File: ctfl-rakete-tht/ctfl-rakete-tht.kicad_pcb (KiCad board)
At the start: 2 copper layers, 99.6 x 99.2 mm, 30 parts, among them J1 Conn_02x03_Odd_Even, SW1 SW_SPDT, U1 ATtiny212-SS

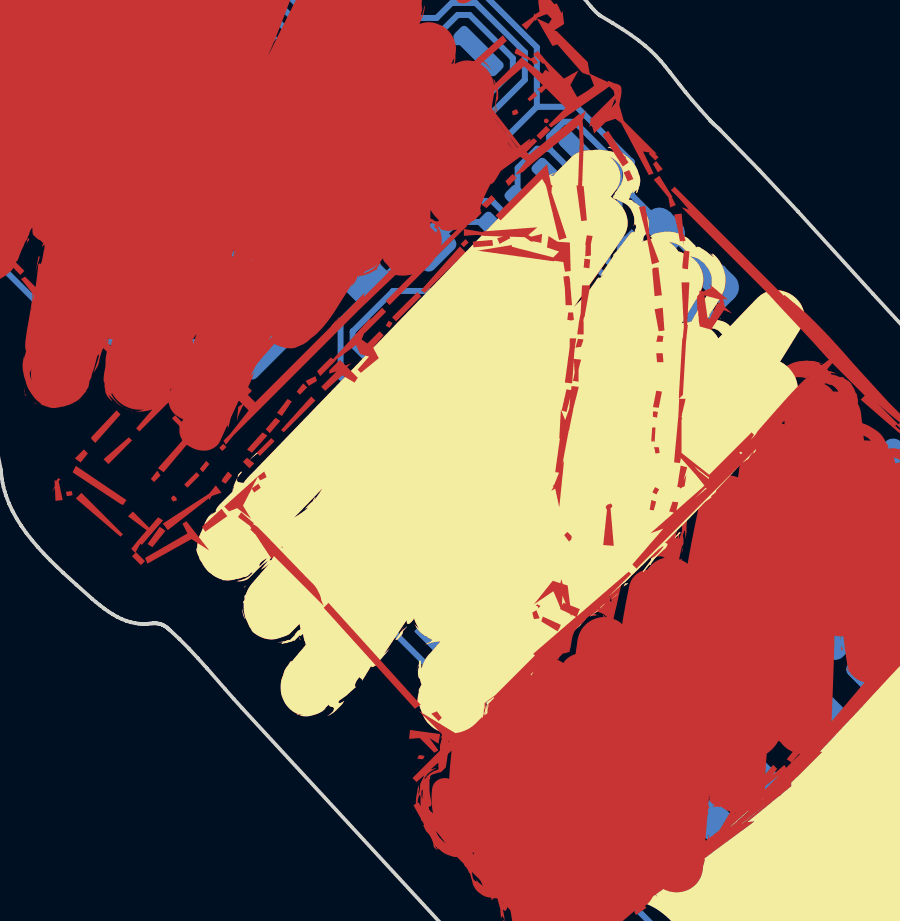
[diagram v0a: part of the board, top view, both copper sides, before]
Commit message: close #3: replaced old programming header with a 1x3 horizontal SMD pin socket footprint (don't let the 3D model of it fool you)
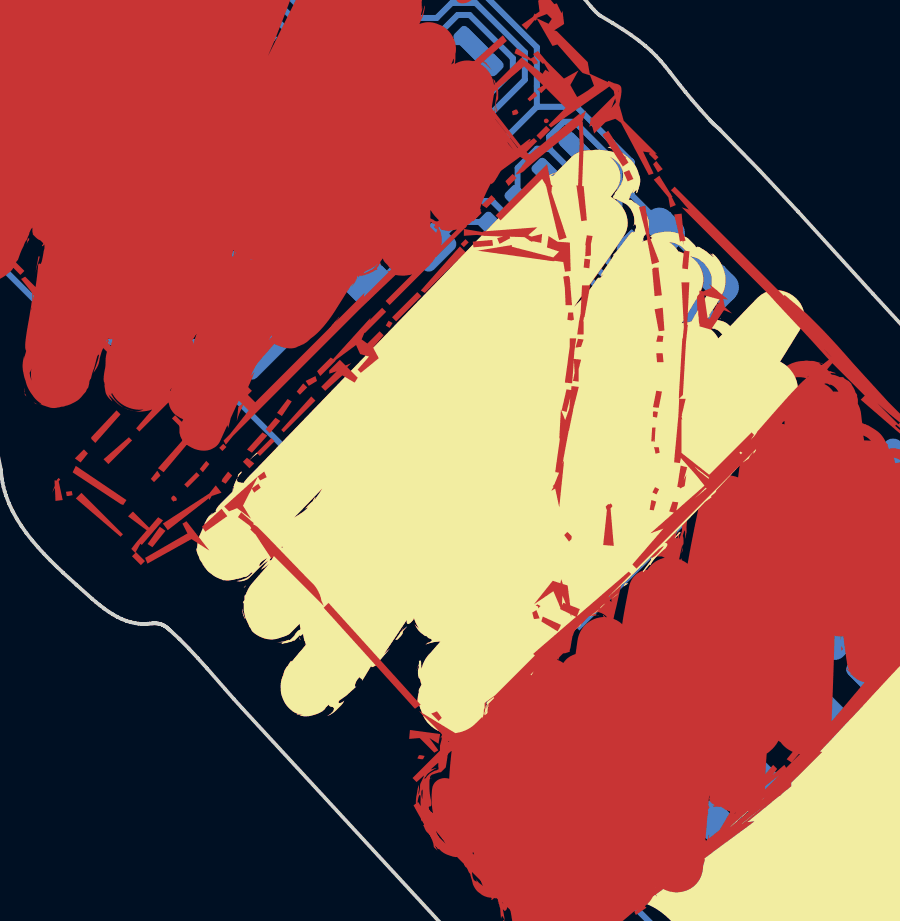
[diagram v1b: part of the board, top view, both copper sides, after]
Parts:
- J1: value Conn_02x03_Odd_Even -> Conn_01x03_Socket; footprint Connector_PinHeader_2.54mm:PinHeader_2x03_P2.54mm_Vertical_SMD -> local:PinSocket_1x03_P2.54mm_Horizontal_SMD
- moved J1 2.61 mm to (156.5, 106.4), turned to 45 degrees
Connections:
- J1 pad 3: unconnected-(J1-Pin_3-Pad3) -> GND
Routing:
- net +3V0: track 60.1 -> 53.7 mm
- net GND: track 194.7 -> 197.9 mm
- net /UPDI_DATA: track 12.2 -> 14.3 mm

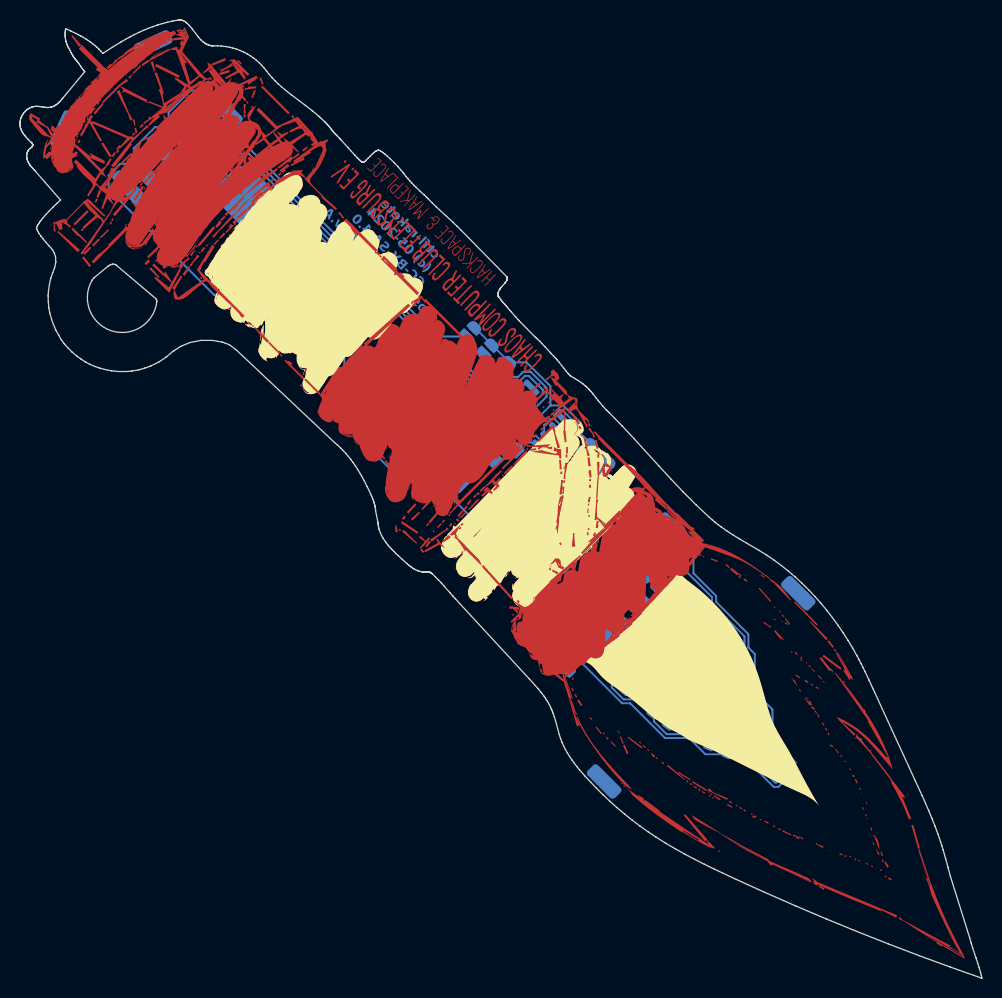
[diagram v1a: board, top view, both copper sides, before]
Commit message: added logo script to mask and silkscreen layer so that it is more legible and added a placeholder for JLCPCBs order number
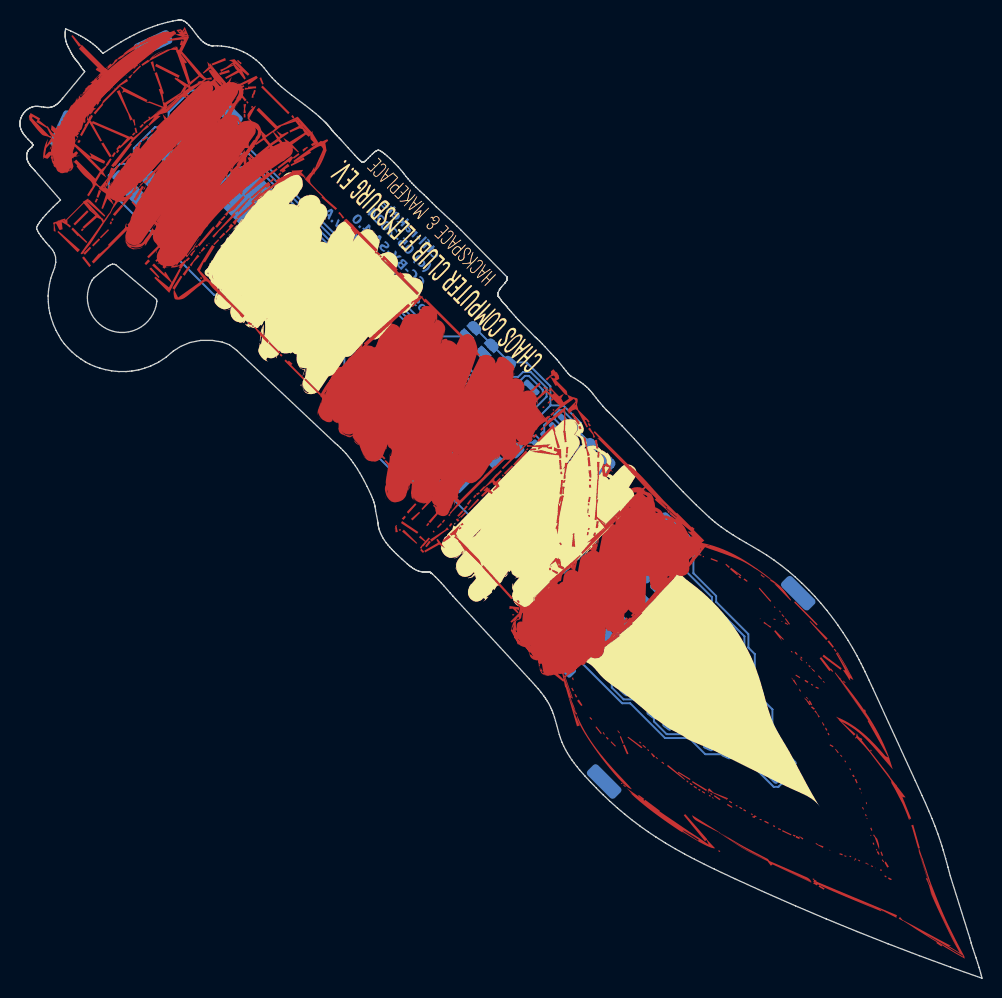
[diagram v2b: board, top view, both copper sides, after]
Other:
- board text added: "JLCJLCJLCJLC"

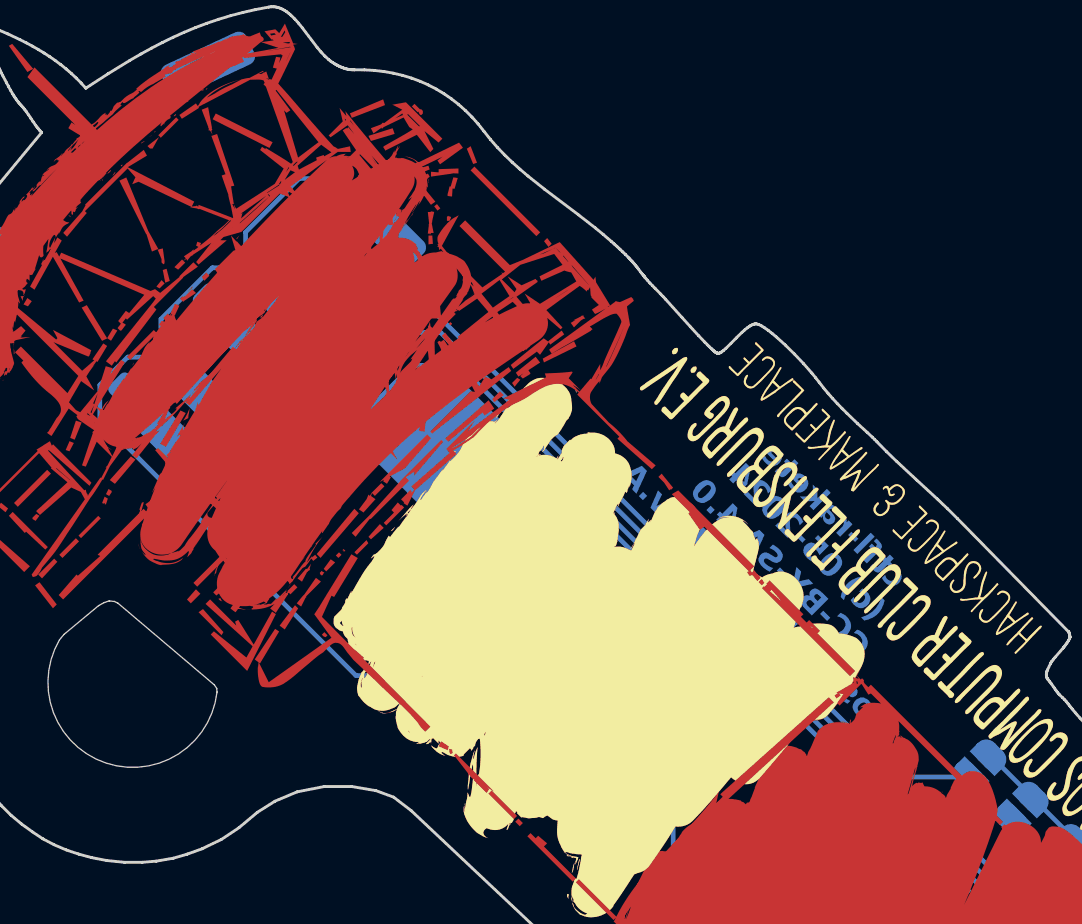
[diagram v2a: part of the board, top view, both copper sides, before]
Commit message: changed revision marking to Rev.B
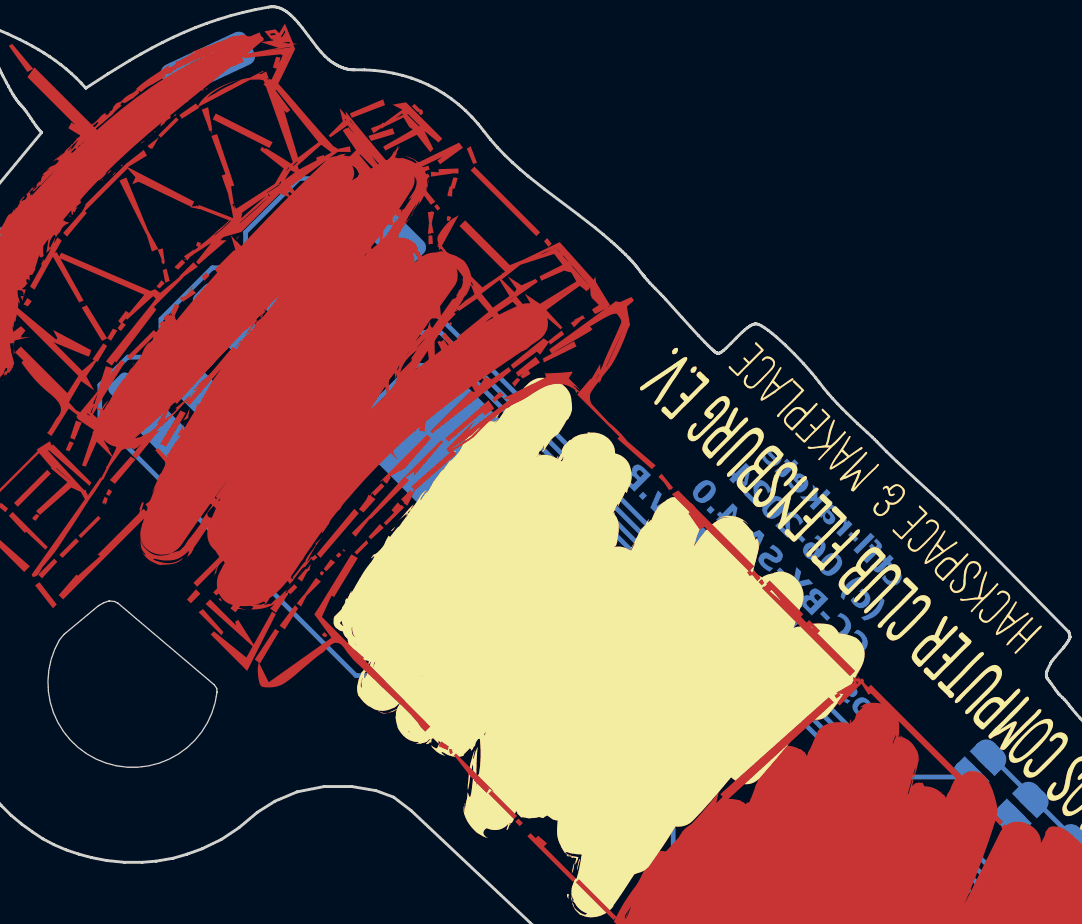
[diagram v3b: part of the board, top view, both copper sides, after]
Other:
- board text added: "ctfl-rakete (c) 06-2024 CC-BY-SA 4.0 Jost Salathé - Rev.B"
- board text removed: "ctfl-rakete (c) 05-2024 CC-BY-SA 4.0 Jost Salathé - Rev.A"
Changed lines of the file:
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@@
 	(title_block
 		(title "ctfl-rakete-tht")
-		(date "2024-06-02")
-		(rev "Rev.A")
+		(date "2024-06-25")
+		(rev "Rev.B")
 		(company "Chaostreff Flensburg")
 		(comment 1 "designed by Jost Salathé")
@@
 		(fp_arc
 			(start -5.450001 8.449999)
-			(mid -8.716433 9.069825)
+			(mid -8.716432 9.069825)
 			(end -10.55541 6.3)
 			(stroke
@@
 			(xy 111.051362 56.051669) (xy 111.051584 56.050536) (xy 111.052193 56.048222) (xy 111.052986 56.045888)
 			(xy 111.053911 56.043584) (xy 111.054916 56.041362) (xy 111.055952 56.039271) (xy 111.056967 56.037364)
-			(xy 111.057913 56.035688) (xy 111.059968 56.032335) (xy 111.059968 56.032335)
+			(xy 111.057913 56.035688) (xy 111.059968 56.032335)
 		)
 		(stroke
@@
 			(xy 105.457424 65.676277) (xy 105.455065 65.679099) (xy 105.452549 65.681774) (xy 105.435649 65.698675)
 			(xy 105.446026 65.677688) (xy 105.451287 65.666714) (xy 105.456658 65.655139) (xy 105.462194 65.642754)
-			(xy 105.46794 65.629347) (xy 105.473946 65.614708) (xy 105.480264 65.598625) (xy 105.480264 65.598625)
+			(xy 105.46794 65.629347) (xy 105.473946 65.614708) (xy 105.480264 65.598625)
 		)
 		(stroke
@@
 		(layer "User.1")
 	)
-	(gr_text "ctfl-rakete\n(c) 05-2024\nCC-BY-SA 4.0\nJost Salathé - Rev.A"
+	(gr_text "ctfl-rakete\n(c) 06-2024\nCC-BY-SA 4.0\nJost Salathé - Rev.B"
 		(at 136.7 75.7 315)
 		(layer "B.Cu")
